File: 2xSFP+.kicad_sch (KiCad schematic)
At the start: 0 parts

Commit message: [#56643] Create buses for interfaces, assign buses to blocks
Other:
- company: (none) -> Antmicro Ltd.
- title: (none) -> Com Express 7 baseboard
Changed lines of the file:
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@@
 (kicad_sch (version 20230121) (generator eeschema)
-  (paper "A4")
+  (paper "A3")
+  (title_block
+    (title "Com Express 7 baseboard")
+    (date "2024-03-22")
+    (rev "1.0.0")
+    (company "Antmicro Ltd.")
+  )
   (hierarchical_label "10GKR_B{10GBaseKR}" (shape input) (at 226.06 99.06 0) (fields_autoplaced)
     (effects (font (size 1.27 1.27)) (justify left))

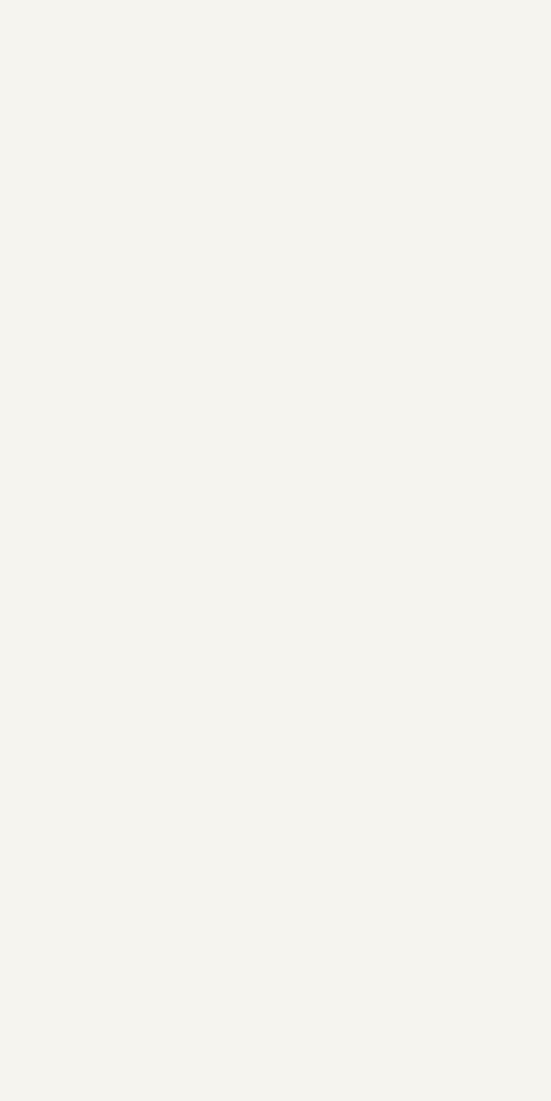
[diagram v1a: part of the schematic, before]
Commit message: [#57056] Create schematics for M.2 and OCuLink connectors
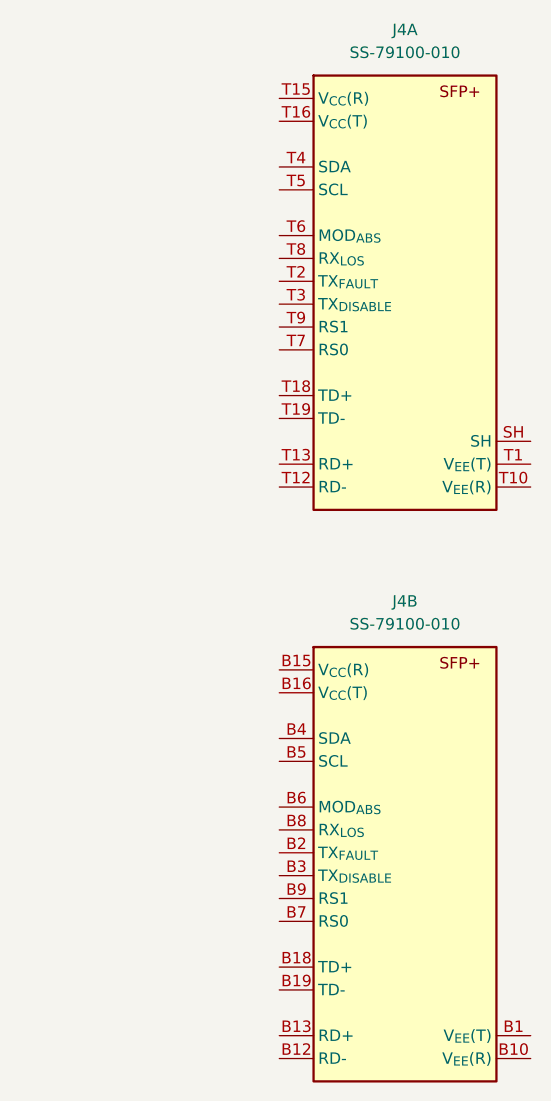
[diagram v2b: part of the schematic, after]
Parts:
- added J4: SFP+_Bel_SS-79100-010, antmicro-footprints:SFP_SS-79100-010, symbol antmicroEdgeConnectors:SFP+_Bel_SS-79100-010
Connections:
- new net: J4.T1 (V_{EE}(T)), J4.T17 (V_{EE}(T)), J4.T20 (V_{EE}(T))
- new net: J4.T10 (V_{EE}(R)), J4.T11 (V_{EE}(R)), J4.T14 (V_{EE}(R))
- new net: J4.B1 (V_{EE}(T)), J4.B17 (V_{EE}(T)), J4.B20 (V_{EE}(T))
- new net: J4.B10 (V_{EE}(R)), J4.B11 (V_{EE}(R)), J4.B14 (V_{EE}(R))
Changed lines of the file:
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@@
     (effects (font (size 1.27 1.27)) (justify left))
   )
+  (symbol (lib_id "antmicroEdgeConnectors:SFP+_Bel_SS-79100-010") (at 309.88 91.44 0) (unit 1)
+    (in_bom yes) (on_board yes) (dnp no) (fields_autoplaced)
+    (property "Reference" "J4" (at 323.85 83.82 0)
+      (effects (font (size 1.27 1.27) (thickness 0.15)))
+    )
+    (property "Value" "SFP+_Bel_SS-79100-010" (at 351.79 104.14 0)
+      (effects (font (size 1.27 1.27) (thickness 0.15)) (justify left bottom) hide)
+    )
+    (property "Footprint" "antmicro-footprints:SFP_SS-79100-010" (at 351.79 106.68 0)
+      (effects (font (size 1.27 1.27) (thickness 0.15)) (justify left bottom) hide)
+    )
+    (property "Datasheet" "https://www.belfuse.com/resources/datasheets/stewartconnector/ds-STW-SFP-cages.pdf" (at 351.79 109.22 0)
+      (effects (font (size 1.27 1.27) (thickness 0.15)) (justify left bottom) hide)
+    )
+    (property "MPN" "SS-79100-010" (at 323.85 86.36 0)
+      (effects (font (size 1.27 1.27) (thickness 0.15)))
+    )
+    (property "Manufacturer" "Bel Fuse" (at 351.79 99.06 0)
+      (effects (font (size 1.27 1.27) (thickness 0.15)) (justify left bottom) hide)
+    )
+    (property "Author" "Antmicro" (at 351.79 111.76 0)
+      (effects (font (size 1.27 1.27) (thickness 0.15)) (justify left bottom) hide)
+    )
+    (property "License" "Apache-2.0" (at 351.79 114.3 0)
+      (effects (font (size 1.27 1.27) (thickness 0.15)) (justify left bottom) hide)
+    )
+    (pin "T4")
+    (pin "B13")
+    (pin "B16")
+    (pin "B15")
+    (pin "B19")
+    (pin "B20")
+    (pin "T11")
+    (pin "B4")
+    (pin "B9")
+    (pin "B18")
+    (pin "B6")
+    (pin "T8")
+    (pin "B12")
+    (pin "B17")
+    (pin "T2")
+    (pin "B14")
+    (pin "B5")
+    (pin "B7")
+    (pin "T19")
+    (pin "B1")
+    (pin "T18")
+    (pin "B8")
+    (pin "T20")
+    (pin "B2")
+    (pin "T17")
+    (pin "T9")
+    (pin "T5")
+    (pin "T15")
+    (pin "T7")
+    (pin "B11")
+    (pin "T6")
+    (pin "B10")
+    (pin "T12")
+    (pin "T3")
+    (pin "T16")
+    (pin "B3")
+    (pin "T1")
+    (pin "T10")
+    (pin "SH")
+    (pin "T13")
+    (pin "T14")
+    (instances
+      (project "com-express-7-baseboard"
+        (path "/1b8c34da-dad5-4b0b-8c4b-45db766c4dfa/bc90cc14-34f1-4905-9b90-ab809e861ec6"
+          (reference "J4") (unit 1)
+        )
+      )
+    )
+  )
+  (symbol (lib_id "antmicroEdgeConnectors:SFP+_Bel_SS-79100-010") (at 309.88 154.94 0) (unit 2)
+    (in_bom yes) (on_board yes) (dnp no) (fields_autoplaced)
+    (property "Reference" "J4" (at 323.85 147.32 0)
+      (effects (font (size 1.27 1.27) (thickness 0.15)))
+    )
+    (property "Value" "SFP+_Bel_SS-79100-010" (at 351.79 167.64 0)
+      (effects (font (size 1.27 1.27) (thickness 0.15)) (justify left bottom) hide)
+    )
+    (property "Footprint" "antmicro-footprints:SFP_SS-79100-010" (at 351.79 170.18 0)
+      (effects (font (size 1.27 1.27) (thickness 0.15)) (justify left bottom) hide)
+    )
+    (property "Datasheet" "https://www.belfuse.com/resources/datasheets/stewartconnector/ds-STW-SFP-cages.pdf" (at 351.79 172.72 0)
+      (effects (font (size 1.27 1.27) (thickness 0.15)) (justify left bottom) hide)
+    )
+    (property "MPN" "SS-79100-010" (at 323.85 149.86 0)
+      (effects (font (size 1.27 1.27) (thickness 0.15)))
+    )
+    (property "Manufacturer" "Bel Fuse" (at 351.79 162.56 0)
+      (effects (font (size 1.27 1.27) (thickness 0.15)) (justify left bottom) hide)
+    )
+    (property "Author" "Antmicro" (at 351.79 175.26 0)
+      (effects (font (size 1.27 1.27) (thickness 0.15)) (justify left bottom) hide)
+    )
+    (property "License" "Apache-2.0" (at 351.79 177.8 0)
+      (effects (font (size 1.27 1.27) (thickness 0.15)) (justify left bottom) hide)
+    )
+    (pin "T4")
+    (pin "B13")
+    (pin "B16")
+    (pin "B15")
+    (pin "B19")
+    (pin "B20")
+    (pin "T11")
+    (pin "B4")
+    (pin "B9")
+    (pin "B18")
+    (pin "B6")
+    (pin "T8")
+    (pin "B12")
+    (pin "B17")
+    (pin "T2")
+    (pin "B14")
+    (pin "B5")
+    (pin "B7")
+    (pin "T19")
+    (pin "B1")
+    (pin "T18")
+    (pin "B8")
+    (pin "T20")
+    (pin "B2")
+    (pin "T17")
+    (pin "T9")
+    (pin "T5")
+    (pin "T15")
+    (pin "T7")
+    (pin "B11")
+    (pin "T6")
+    (pin "B10")
+    (pin "T12")
+    (pin "T3")
+    (pin "T16")
+    (pin "B3")
+    (pin "T1")
+    (pin "T10")
+    (pin "SH")
+    (pin "T13")
+    (pin "T14")
+    (instances
+      (project "com-express-7-baseboard"
+        (path "/1b8c34da-dad5-4b0b-8c4b-45db766c4dfa/bc90cc14-34f1-4905-9b90-ab809e861ec6"
+          (reference "J4") (unit 2)
+        )
+      )
+    )
+  )
 )

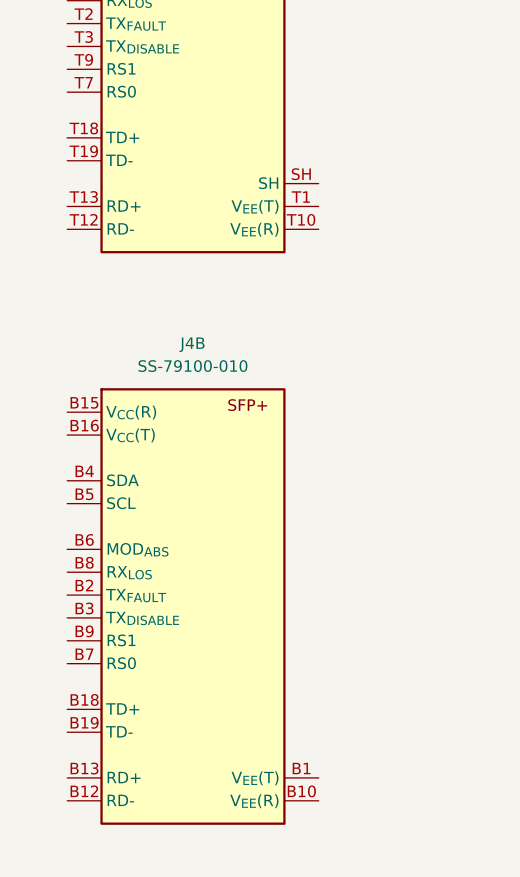
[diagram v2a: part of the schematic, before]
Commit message: [#57056] Update top sheet, update sheet's dates
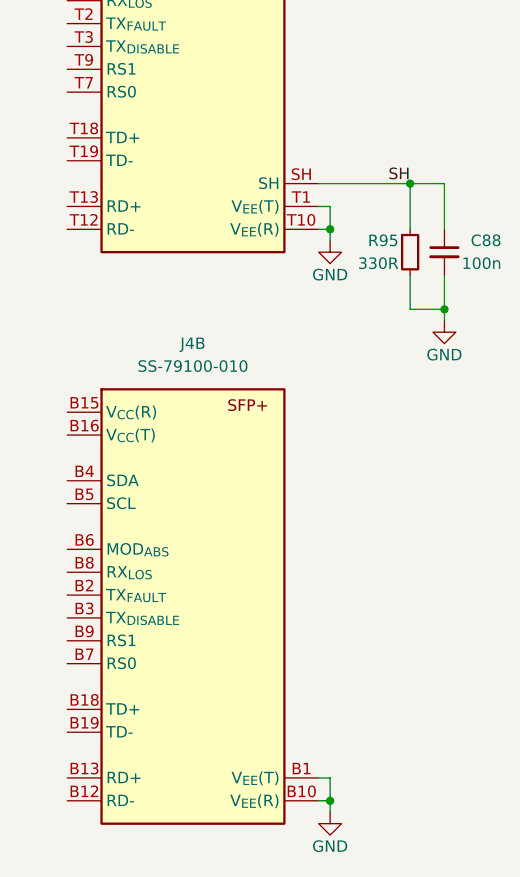
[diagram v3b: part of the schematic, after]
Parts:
- added C88: C_100n_0402, antmicro-footprints:C_0402_1005Metric, symbol antmicroCapacitors0402:C_100n_0402
- added R95: R_330R_0402, antmicro-footprints:R_0402_1005Metric, symbol antmicroResistors0402:R_330R_0402
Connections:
- net SH: now reaches J4.SH
- net SH: now also C88.1, R95.1
- net GND: now reaches J4.T1 (V_{EE}(T)), J4.T17 (V_{EE}(T)), J4.T20 (V_{EE}(T))
- net GND: now also J4.B1 (V_{EE}(T)), J4.B10 (V_{EE}(R)), J4.B11 (V_{EE}(R)), J4.B14 (V_{EE}(R)), J4.B17 (V_{EE}(T)), J4.B20 (V_{EE}(T)), J4.T10 (V_{EE}(R)), J4.T11 (V_{EE}(R)), J4.T14 (V_{EE}(R)), C88.2, R95.2

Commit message: [#57498] Add KR/SFP+
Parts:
- added C43, C44, C89, C90: C_100n_0402, antmicro-footprints:C_0402_1005Metric, symbol antmicroCapacitors0402:C_100n_0402
- added C47, C50: C_22u_0603, antmicro-footprints:C_0603_1608Metric, symbol antmicroCapacitors0603:C_22u_0603
- added R142, R143, R147, R149, R152, R153, R158, R159, R160, R161: R_0R_0402, antmicro-footprints:R_0402_1005Metric, symbol antmicroResistors0402:R_0R_0402
- added R144, R145, R146, R148, R154, R155, R156, R157: R_1k_0402, antmicro-footprints:R_0402_1005Metric, symbol antmicroResistors0402:R_1k_0402
- added TP38, TP39, TP43, TP45: TP_0.75mm_SMD, antmicro-footprints:TP_SMD_0.75mm, symbol antmicroTestPoints:TP_0.75mm_SMD
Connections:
- net GND: now also C43.1, C44.1, C47.1, C50.1, C89.1, C90.1, R147.2, R149.2, R158.2, R159.2
- net SFI0.RX-: now reaches J4.T12 (RD-)
- net SFI0.RX+: now reaches J4.T13 (RD+)
- net +3V3: now reaches J4.T15 (V_{CC}(R))
- net +3V3: now also J4.B15 (V_{CC}(R)), J4.B16 (V_{CC}(T)), J4.T16 (V_{CC}(T)), C43.2, C44.2, C47.2, C50.2, C89.2, C90.2, R144.2, R145.2, R146.2, R148.2, R154.2, R155.2, R156.2, R157.2
- net SFI0.TX+: now reaches J4.T18 (TD+)
- net SFI0.TX-: now reaches J4.T19 (TD-)
- net at J4.T2 (TX_{FAULT}): now also R145.1, TP39.1
- net at J4.T3 (TX_{DISABLE}): now also R147.1
- net SDA0: now reaches J4.T4 (SDA)
- net SDA0: now also R142.2
- net SCL0: now reaches J4.T5 (SCL)
- net SCL0: now also R143.2
- net at J4.T6 (MOD_{ABS}): now also R148.1, R160.2
- net at J4.T7 (RS0): now also R146.1
- net at J4.T8 (RX_{LOS}): now also R144.1, TP38.1
- net at J4.T9 (RS1): now also R149.1
- net SFI1.RX-: now reaches J4.B12 (RD-)
- net SFI1.RX+: now reaches J4.B13 (RD+)
- net SFI1.TX+: now reaches J4.B18 (TD+)
- net SFI1.TX-: now reaches J4.B19 (TD-)
- net at J4.B2 (TX_{FAULT}): now also R155.1, TP43.1
- net at J4.B3 (TX_{DISABLE}): now also R158.1
- net SDA1: now reaches J4.B4 (SDA)
- net SDA1: now also R152.2
- net SCL1: now reaches J4.B5 (SCL)
- net SCL1: now also R153.2
- net at J4.B6 (MOD_{ABS}): now also R157.1, R161.2
- net at J4.B7 (RS0): now also R154.1
- net at J4.B8 (RX_{LOS}): now also R156.1, TP45.1
- net at J4.B9 (RS1): now also R159.1
- new net I2C_{SFP0}.SCL: R143.1
- new net I2C_{SFP0}.SDA: R142.1
- new net I2C_{SFP1}.SCL: R153.1
- new net I2C_{SFP1}.SDA: R152.1
- new net MOD0_ABS: R160.1
- new net MOD1_ABS: R161.1
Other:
- added sheet KR to SFI #1 (kr_sfi.kicad_sch)
- added sheet KR to SFI #2 (kr_sfi.kicad_sch)
- moved on the sheet: J4B
